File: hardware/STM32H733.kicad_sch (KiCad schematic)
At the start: 84 parts, among them IC1 AT7456E, J1 USB, J2 DJI, J3 SWD, J5 Conn_01x06_MountingPin, J7 GPS, J8 ESC, J9 ELRS, U1 STM32H733VGTx, U2 ICM-42688-P, U3 TLV75733PDBV, U4 TJA1051TK-3, U5 BMP280, U6 W25Q128JVP, U7 LMR51430, U8 LMR51430, Y1 Resonator_Small, Y2 27MHz

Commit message: Flight Controller:
Almost Done With the PCB design Except the Leds
and Few Peripherals Pad for external Sensors
and modules

Signed-off-by: Asraful Islam Taj <asraful.islam.taj@gmail.com>
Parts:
- removed D1: BAT54C, Package_TO_SOT_SMD:SOT-23, symbol Diode:BAT54C
- removed FB1: 600 Ohm 100MHz, symbol Device:FerriteBead_Small
- removed U6: W25Q128JVP, Package_SON:WSON-8-1EP_6x5mm_P1.27mm_EP3.4x4.3mm, symbol Memory_Flash:W25Q128JVP
- added C23: .1u, Capacitor_SMD:C_0402_1005Metric, symbol Device:C_Small
- added C24: 33nF, Capacitor_SMD:C_0402_1005Metric, symbol Device:C_Small
- added D3, D5: SS34, Diode_SMD:D_SMA, symbol Diode:SS34
- added D4: SMAJ36A, Diode_SMD:D_SMA, symbol Diode:SMAJ36A
- added J10: CH, TestPoint:TestPoint_Pad_1.0x1.0mm, symbol Connector:Conn_01x01_Pin
- added J11: CL, TestPoint:TestPoint_Pad_1.0x1.0mm, symbol Connector:Conn_01x01_Pin
- added J4, J6: Conn_01x01_Pin, TestPoint:TestPoint_Pad_1.5x1.5mm, symbol Connector:Conn_01x01_Pin
- added Q1: SS8050, Package_TO_SOT_SMD:SOT-23, symbol Transistor_BJT:SS8050
- added R15: 1K, Resistor_SMD:R_0402_1005Metric, symbol Device:R_Small
- added R16: 100K, Resistor_SMD:R_0402_1005Metric, symbol Device:R_Small
- added R17: 10K, Resistor_SMD:R_0402_1005Metric, symbol Device:R_Small
- added U6: W25Q128JVS, Package_SO:SOIC-8_5.3x5.3mm_P1.27mm, symbol Memory_Flash:W25Q128JVS
- IC1: footprint user:SOP65P640X120-29N -> User:SOP65P640X120-29N
- J5: value Conn_01x06_MountingPin -> VTX
- U2: footprint user:PQFN50P300X250X97-14N -> User:PQFN50P300X250X97-14N
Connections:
- net +3.3VA is gone; now on net +3.3V: C12.2, C13.2, U1.20 (VREF+), U1.21 (VDDA)
- net ACD_CURR is gone; now on net ADC_CURR: J8.8 (Pin_8)
- net OSD_CS is gone; now on net OSD_NSS2: IC1.8 (~{CS})
- net OSD_MISO is gone; now on net OSD_MISO2: IC1.11 (SDOUT)
- net OSD_MOSI is gone; now on net OSD_MOSI2: IC1.9 (SDIN)
- net SBUS is gone; now on net SBUS_RX4: J2.6 (Pin_6)
- net SCK2 is gone; now on net OSD_SCK2: U1.52 (PB13)
- net SCL2 is gone; now on net BARO_SCL2: U1.46 (PB10)
- net SDA2 is gone; now on net BARO_SDA2: U1.47 (PB11)
- net TLM is gone; now on net TLM_RX1: J8.7 (Pin_7)
- net +3.3V: now also C23.2, U6.3 (~{WP}/IO_{2}), U6.7 (~{HOLD}/~{RESET}/IO_{3}), U6.8 (VCC)
- net +5VUSB: now also D5.2 (A)
- net +B5V: now also C39.2, D3.2 (A); no longer C17.2, C20.2, C21.2, C22.2, C39.1, C47.1, IC1.21 (AVDD), IC1.24 (PVDD), IC1.3 (DVDD), J5.3 (Pin_3), J7.2 (Pin_2), J9.3 (Pin_3), R10.1, R7.1, R8.1, R9.1, U4.3 (VCC)
- net CANH: now also J10.1 (Pin_1)
- net CANL: now also J11.1 (Pin_1)
- net FLASH_MISO3: now also U6.2 (DO/IO_{1})
- net FLASH_MOSI3: now also U6.5 (DI/IO_{0})
- net FLASH_NSS3: now also U6.1 (~{CS})
- net FLASH_SCK3: now also U6.6 (CLK)
- net GND: now also C39.1, C23.1, C24.2, D4.2 (A2), Q1.2 (E), R17.1, U6.4 (GND); no longer C39.2
- net VBAT: now also D4.1 (A1), R16.2
- net ADC_CURR: now reaches U1.15 (PC0)
- net VBAT_ADC: now reaches U1.16 (PC1)
- net VBAT_ADC: now also C24.1, R16.1, R17.2
- net BUZZ_GPIO: now reaches U1.3 (PE4)
- net BUZZ_GPIO: now also R15.1
- net GPS_SCL4: now reaches U1.59 (PD12)
- net GPS_SCL4: now also J7.5 (Pin_5), R12.2
- net GPS_SDA4: now reaches U1.60 (PD13)
- net GPS_SDA4: now also J7.6 (Pin_6), R11.2
- net 5V_SYS: now reaches C3.1, U3.1 (IN), U3.3 (EN)
- net 5V_SYS: now also C17.2, C20.2, C21.2, C22.2, C47.1, IC1.21 (AVDD), IC1.24 (PVDD), IC1.3 (DVDD), J5.3 (Pin_3), J7.2 (Pin_2), J9.3 (Pin_3), R10.1, R7.1, R8.1, R9.1, U4.3 (VCC), D3.1 (K), D5.1 (K), J6.1 (Pin_1)
- net BARO_I2C2_SCL renamed BARO_SCL2
- net BARO_I2C2_SDA renamed BARO_SDA2
- removed net GPS_I2C1_SCL: J7.5 (Pin_5), R11.2
- removed net GPS_I2C1_SDA: J7.6 (Pin_6), R12.2
- net GPS_USART1_RX renamed GPS_USART3_RX
- net GPS_USART3_RX: now also J7.4 (Pin_4); no longer J7.3 (Pin_3)
- net GPS_USART1_TX renamed GPS_USART3_TX
- net GPS_USART3_TX: now also J7.3 (Pin_3); no longer J7.4 (Pin_4)
- net MISO2 renamed OSD_MISO2
- net MOSI2 renamed OSD_MOSI2
- net NSS2 renamed OSD_NSS2
- net OSD_SCK renamed OSD_SCK2
- net RX1 renamed TLM_RX1
- net RX4 renamed SBUS_RX4
- new net: Q1.1 (B), R15.2
- new net BUZZ: J4.1 (Pin_1), Q1.3 (C)
- no-connect marks 15 -> 51
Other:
- note added: "BAT Voltage ADC"
- note added: "BUZZER"
- note added: "Bypass Caps"
- note added: "I2C Pullups"
- note added: "INP SRC Select"
- note added: "JST Connectors"
- note added: "Mounting Hole"
- moved on the sheet: C15, C16, C17, C18, C19, C20, C21, C22, C3, C36, C37, C38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
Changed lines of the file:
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@@
 	(generator "eeschema")
 	(generator_version "10.0")
-	(paper "A2")
+	(paper "A3")

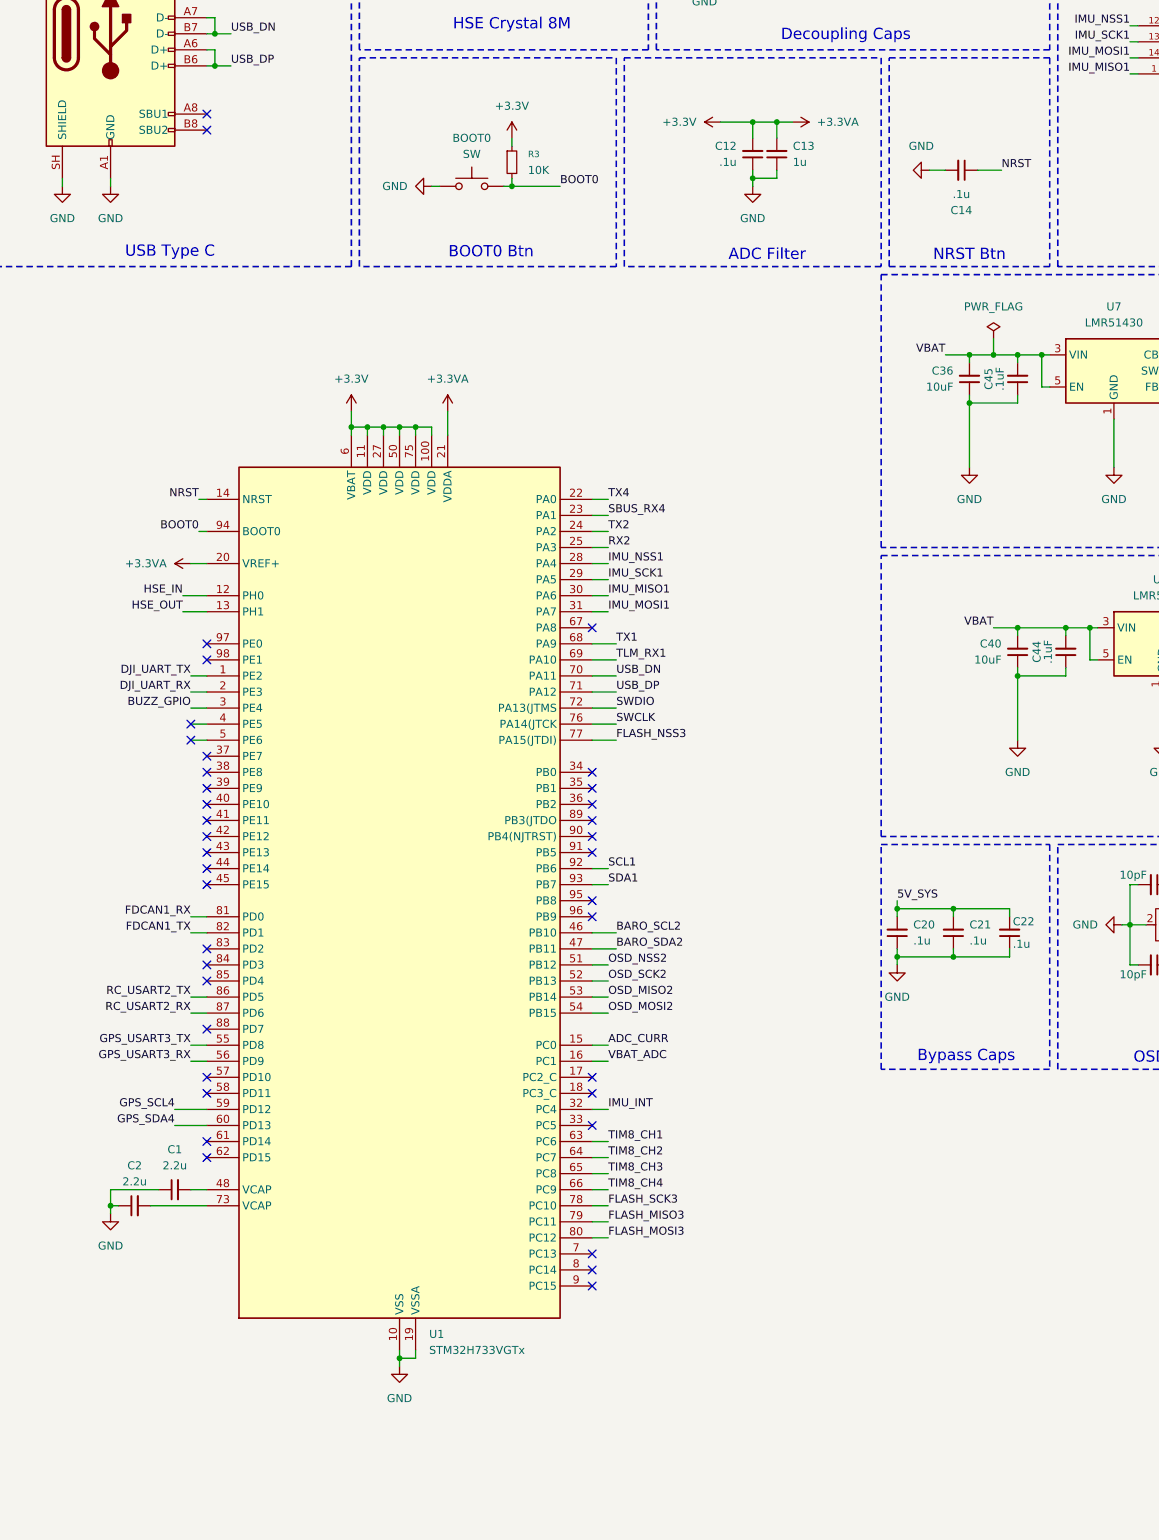
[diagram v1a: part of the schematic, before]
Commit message: Nebula H7: V 0.1
need to add some indicator led

Signed-off-by: Asraful Islam Taj <asraful.islam.taj@gmail.com>
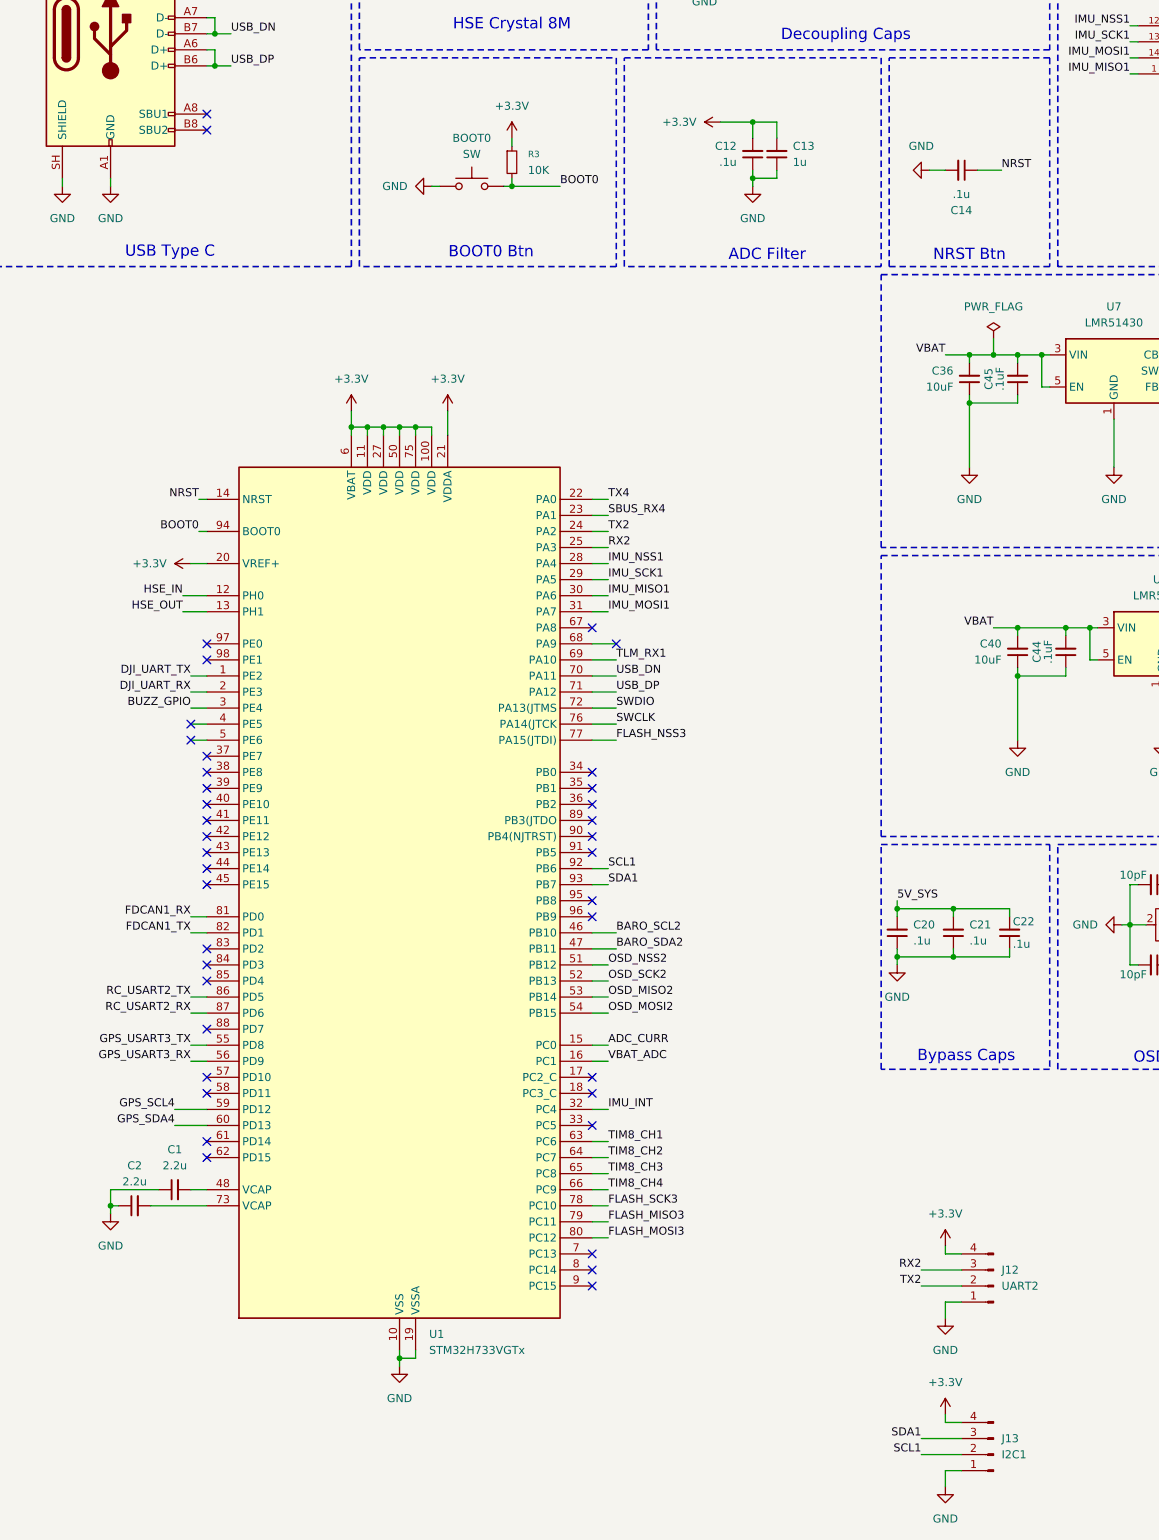
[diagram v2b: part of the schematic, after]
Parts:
- added J12: UART2, Custom:ConnPadx04, symbol Connector:Conn_01x04_Pin
- added J13: I2C1, Custom:ConnPadx04, symbol Connector:Conn_01x04_Pin
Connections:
- net +3.3V: now also J12.4 (Pin_4), J13.4 (Pin_4)
- net GND: now also J12.1 (Pin_1), J13.1 (Pin_1)
- net RX2: now also J12.3 (Pin_3)
- net SCL1: now also J13.2 (Pin_2)
- net SDA1: now also J13.3 (Pin_3)
- net TX2: now also J12.2 (Pin_2)
- net TX1: no longer names the net of U1.68 (PA9)
- no-connect marks 51 -> 52
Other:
- company: (none) -> Asraful Islam Taj
- title: (none) -> Nebula H7
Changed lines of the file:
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@@
 	(generator_version "10.0")
 	(paper "A3")
+	(title_block
+		(title "Nebula H7")
+		(date "2026-05-14")
+		(rev "0.1")
+		(company "Asraful Islam Taj")
+		(comment 1 "https://github.com/segfaultdev")
+	)
